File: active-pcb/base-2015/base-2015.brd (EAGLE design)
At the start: 50.5 x 64.8 mm, 5 parts, among them X1 MINI-USB-32005-201

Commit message: minor changes
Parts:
- renumbered KIT1 to MBED

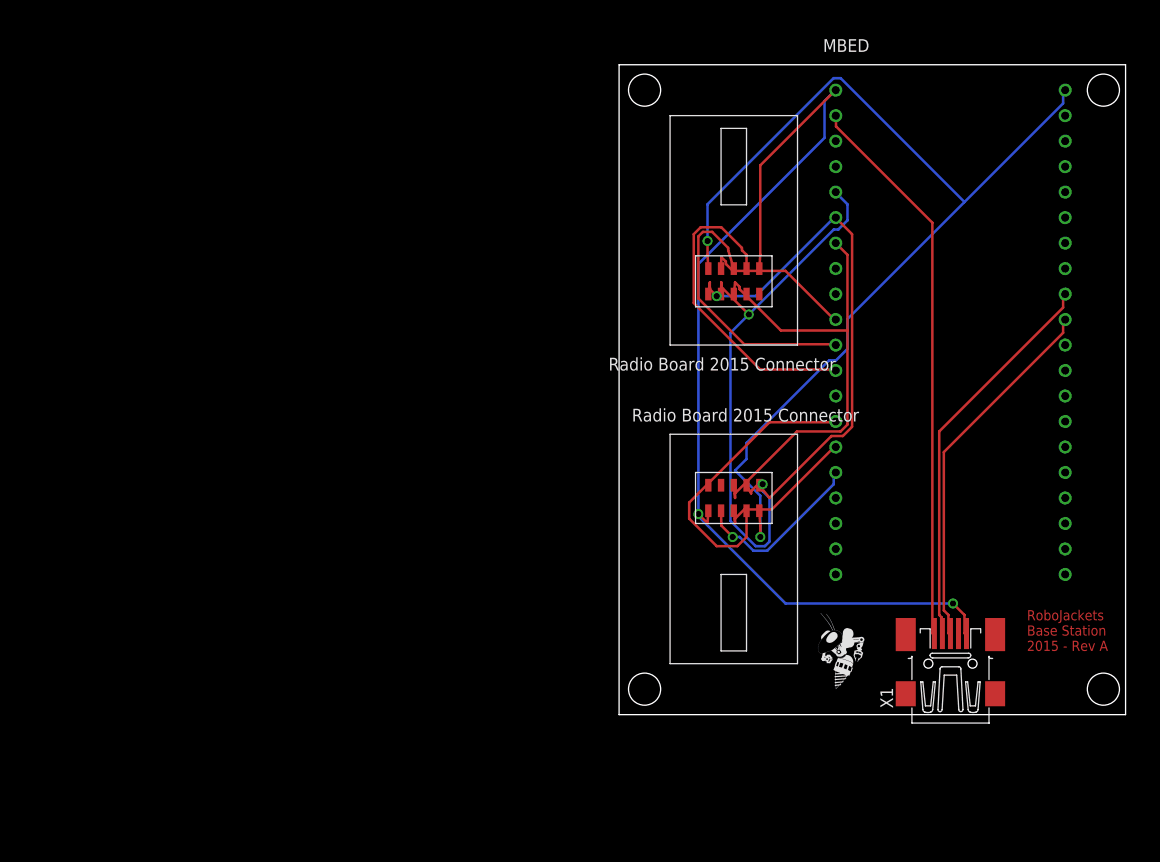
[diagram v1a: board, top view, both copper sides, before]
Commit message: updated radio board footprint, shifting around pcb items
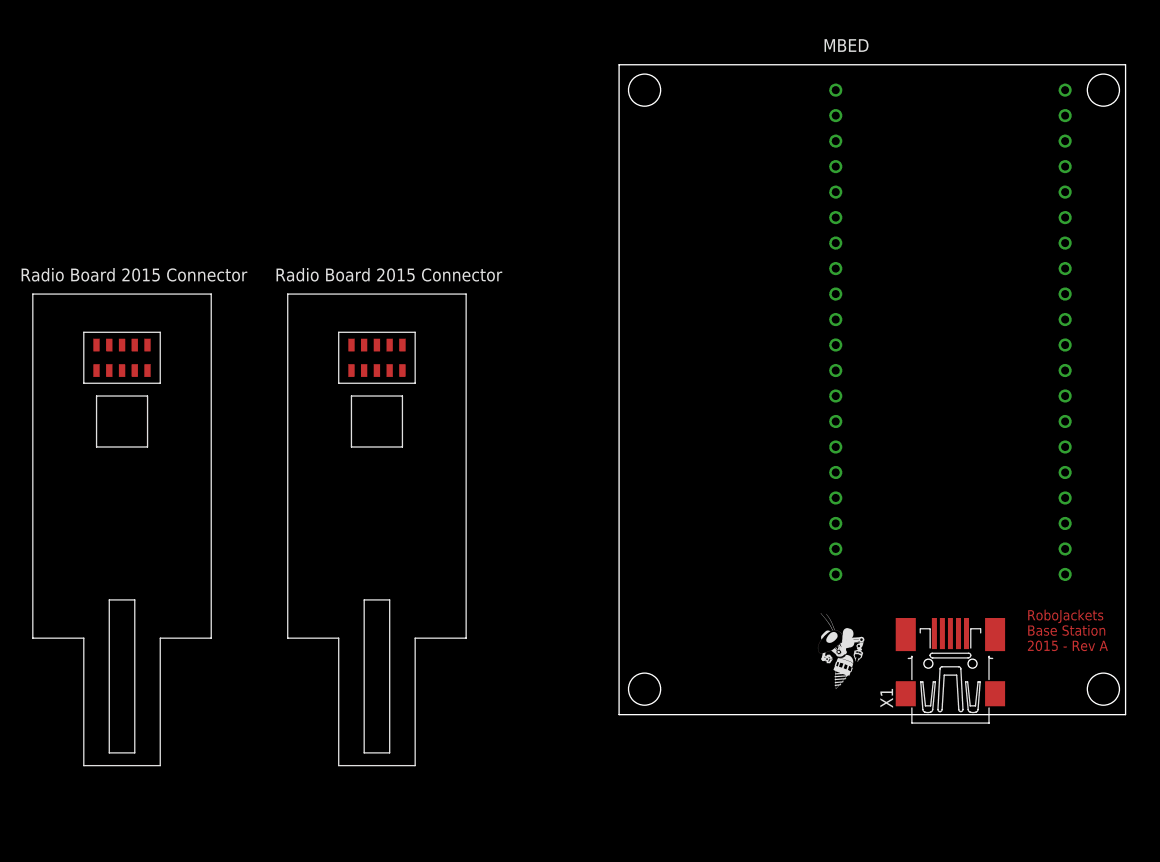
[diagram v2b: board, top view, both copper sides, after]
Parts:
- U$1, U$2: value RADIO201500CONNECTOR -> RADIOBOARD2015CONNECTOR; device radio-2015-connector:CONNPACKAGE -> radio-2015-connector:RADIOBOARD2015CONNECTOR
- moved U$2 66.2 mm to (-30.5, 49.5), turned to 0 degrees
- moved U$1 38.2 mm to (-5.08, 49.5)
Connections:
- net N$10: now also U$1.CSN; no longer U$2.CSN
- net N$12: now also U$1.RESET; no longer U$2.RESET
- net N$13: now also U$2.INT; no longer U$1.INT
- net N$14: now also U$2.RESET; no longer U$1.RESET
- net N$4: now also U$2.CSN; no longer U$1.CSN
- net N$9: now also U$1.INT; no longer U$2.INT
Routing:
- net N$8: track 104.5 -> 0.00 mm, vias 2 -> 0
- net N$16: track 104.2 -> 0.00 mm, vias 2 -> 0
- net N$2: track 57.6 -> 0.00 mm, vias 2 -> 0
- net N$5: track 55.8 -> 0.00 mm
- net N$3: track 52.2 -> 0.00 mm, vias 1 -> 0
- net N$17: track 48.8 -> 0.00 mm
- net N$6: track 39.2 -> 0.00 mm
- net N$7: track 36.7 -> 0.00 mm
- net N$9: track 32.0 -> 0.00 mm
- net N$14: track 29.4 -> 0.00 mm
- net N$10: track 27.7 -> 0.00 mm
- net N$13: track 17.8 -> 0.00 mm, vias 1 -> 0
- net N$12: track 15.2 -> 0.00 mm
- net N$4: track 14.7 -> 0.00 mm

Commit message: re-arranged board
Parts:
- moved X1 58.7 mm to (33.0, 72.4), turned to 270 degrees
- moved U$2 52.1 mm to (6.35, 12.7), turned to 90 degrees
- moved U$1 22.6 mm to (12.7, 35.6), turned to 180 degrees
- moved MBED 21.6 mm to (33.0, 52.1)
- moved U$3 12.7 mm to (43.2, 2.54)
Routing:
- net N$16: track 0.00 -> 93.4 mm
- net N$8: track 0.00 -> 81.1 mm, vias 0 -> 2
- net N$17: track 0.00 -> 68.7 mm, vias 0 -> 2
- net N$2: track 0.00 -> 59.4 mm
- net N$3: track 0.00 -> 53.0 mm
- net N$14: track 0.00 -> 34.4 mm
- net N$4: track 0.00 -> 32.8 mm
- net N$13: track 0.00 -> 32.3 mm
- net N$5: track 0.00 -> 27.6 mm
- net N$7: track 0.00 -> 20.8 mm
- net N$12: track 0.00 -> 20.5 mm
- net N$6: track 0.00 -> 17.9 mm
- net N$10: track 0.00 -> 17.5 mm
- net N$9: track 0.00 -> 14.8 mm
- added copper zone on layer 1, net GND
- added copper zone on layer 16, net GND
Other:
- board size 50.5 x 64.8 mm -> 53 x 78.7 mm
